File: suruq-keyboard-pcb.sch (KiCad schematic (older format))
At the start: 19 parts

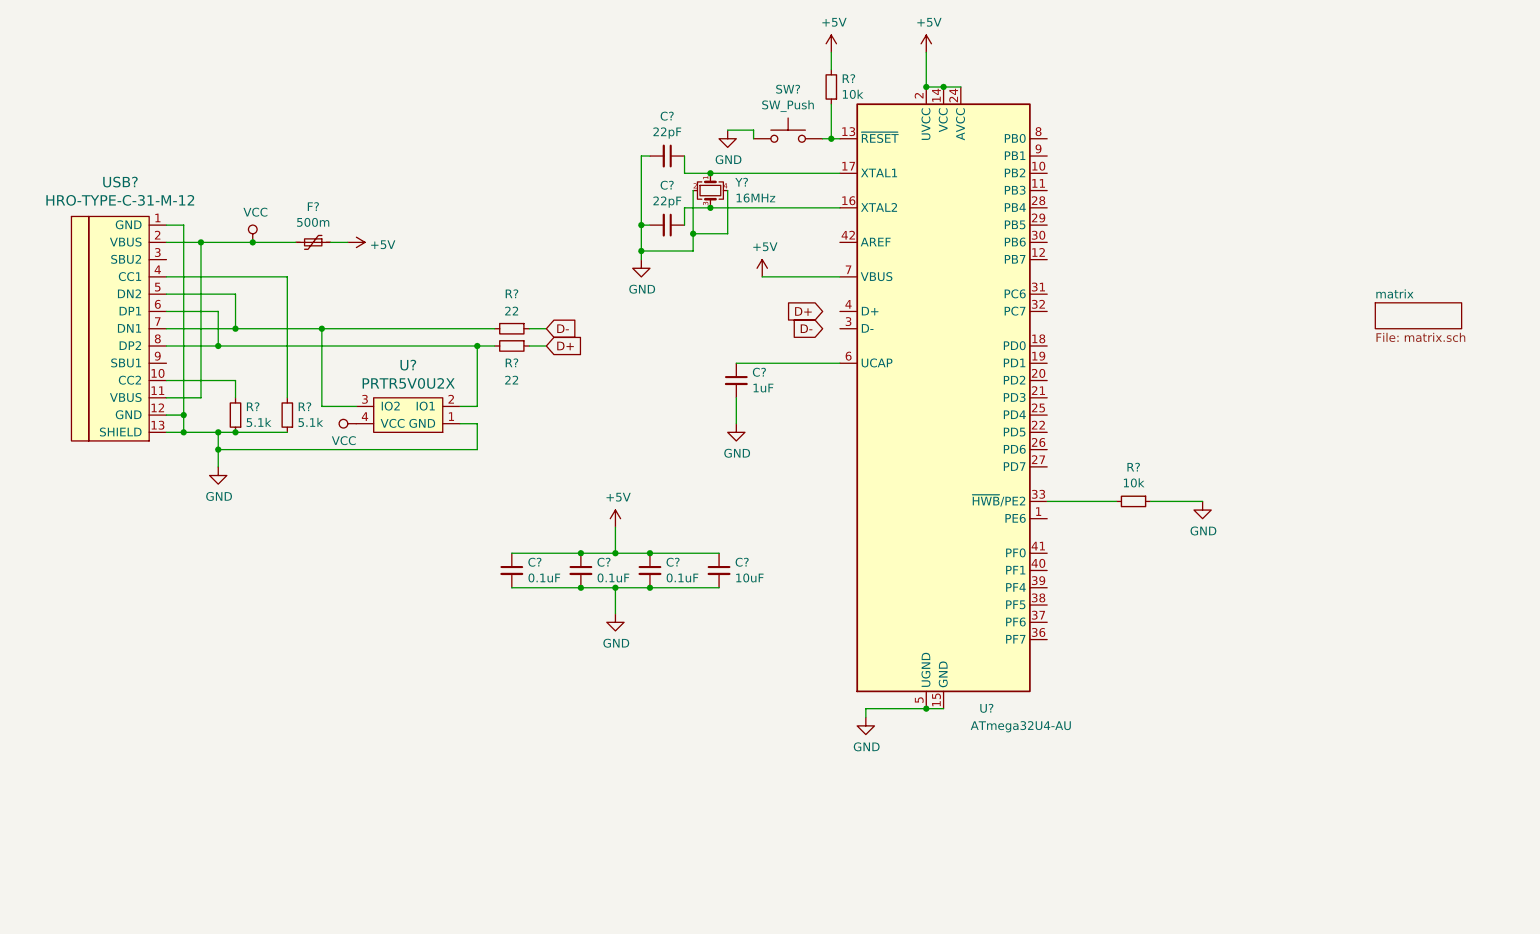
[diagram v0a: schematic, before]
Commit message: change layout and matrix
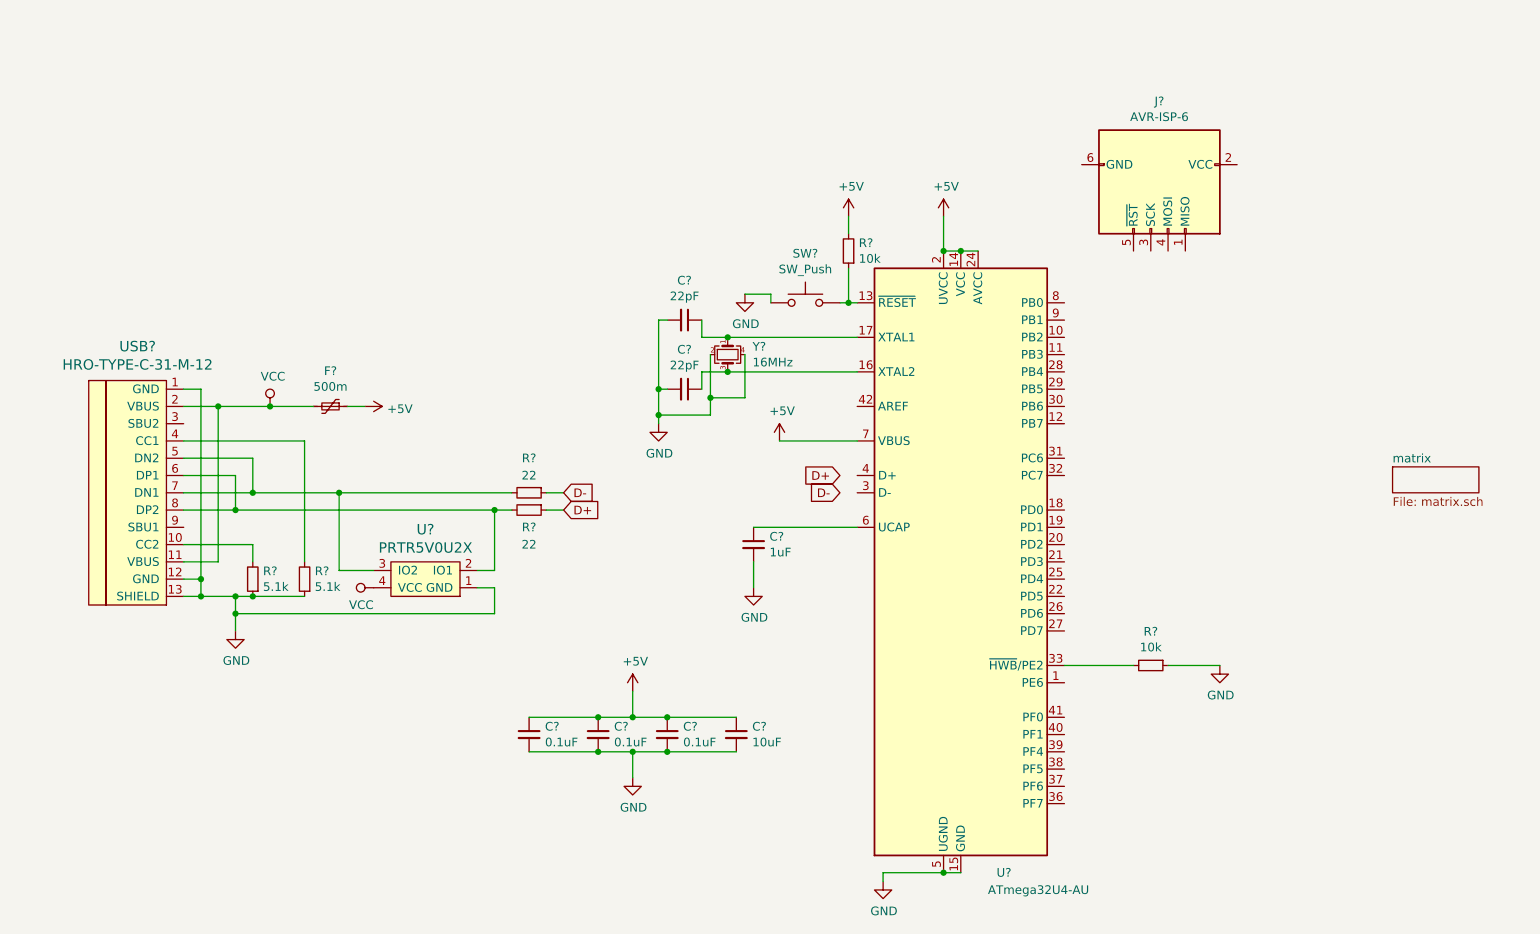
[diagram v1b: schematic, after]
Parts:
- added J?: AVR-ISP-6, symbol Connector:AVR-ISP-6
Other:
- moved on the sheet: C?, F?, R?, SW?, U?, USB?, Y?

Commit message: pcb layout routing WIP
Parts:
- C1, C2, C3, C4, C5, C6, C7: renamed from C?; footprint (none) -> Capacitor_SMD:C_0805_2012Metric_Pad1.15x1.40mm_HandSolder
- F1: renamed from F?; footprint (none) -> Fuse:Fuse_1206_3216Metric_Pad1.42x1.75mm_HandSolder
- J1: renamed from J?; footprint (none) -> random-keyboard-parts:Reset_Pretty-Mask
- R1, R2, R3, R4, R5, R6: renamed from R?; footprint (none) -> Resistor_SMD:R_0805_2012Metric_Pad1.15x1.40mm_HandSolder
- SW65: renamed from SW?; footprint (none) -> Button_Switch_Keyboard:SW_Cherry_MX_1.00u_PCB
- U1: renamed from U?; footprint (none) -> random-keyboard-parts:SOT143B
- USB1: renamed from USB?; footprint (none) -> Type-C:HRO-TYPE-C-31-M-12-HandSoldering
- Y1: renamed from Y?; footprint (none) -> Crystal:Crystal_SMD_3225-4Pin_3.2x2.5mm_HandSoldering
- gave numbers to parts that had none: 1
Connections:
- net +5V: now also J1.2 (VCC)
- net D+: now also U2.4 (D+)
- net D-: now also U2.3 (D-)
- net GND: now also J1.6 (GND)
- net row0: now reaches U2.1 (PE6)
- net rot_out: now reaches U2.11 (PB3)
- net Reset: now reaches R5.1, SW65.2, U2.13 (~RESET)
- net Reset: now also J1.5 (~RST)
- net fad_out: now reaches U2.18 (PD0)
- net col8: now reaches U2.19 (PD1)
- net col9: now reaches U2.20 (PD2)
- net col10: now reaches U2.21 (PD3)
- net col11: now reaches U2.22 (PD5)
- net col12: now reaches U2.25 (PD4)
- net col13: now reaches U2.26 (PD6)
- net col14: now reaches U2.27 (PD7)
- net col0: now reaches U2.28 (PB4)
- net col1: now reaches U2.29 (PB5)
- net col2: now reaches U2.30 (PB6)
- net col3: now reaches U2.31 (PC6)
- net col4: now reaches U2.32 (PC7)
- net col6: now reaches U2.36 (PF7)
- net col5: now reaches U2.37 (PF6)
- net row1: now reaches U2.38 (PF5)
- net row4: now reaches U2.39 (PF4)
- net row3: now reaches U2.40 (PF1)
- net row2: now reaches U2.41 (PF0)
- net col7: now reaches U2.8 (PB0)
- net DN: now reaches R3.2, U1.3 (IO2), USB1.5 (DN2), USB1.7 (DN1)
- net DP: now reaches R4.2, U1.2 (IO1), USB1.6 (DP1), USB1.8 (DP2)
- net MISO: now reaches J1.1 (MISO)
- net SCK: now reaches J1.3 (SCK)
- net MOSI: now reaches J1.4 (MOSI)
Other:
- moved on the sheet: F1, J1, R5, SW65

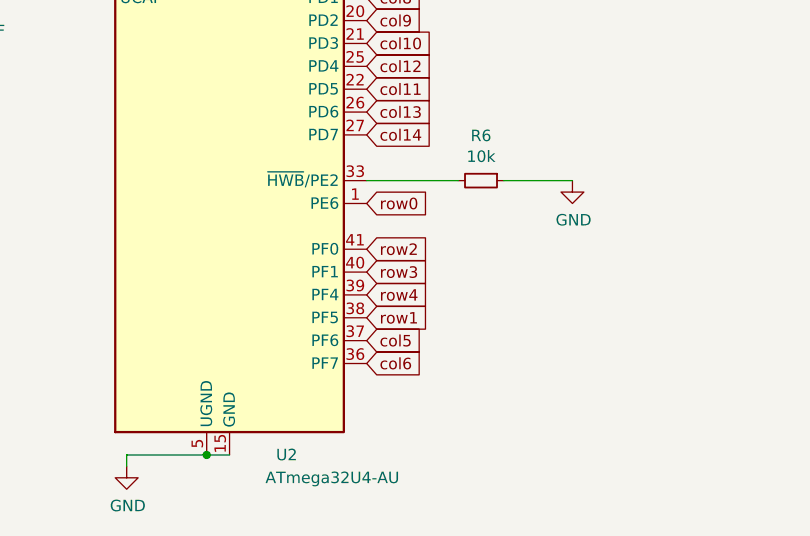
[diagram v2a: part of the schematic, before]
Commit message: routing gauche et MCU
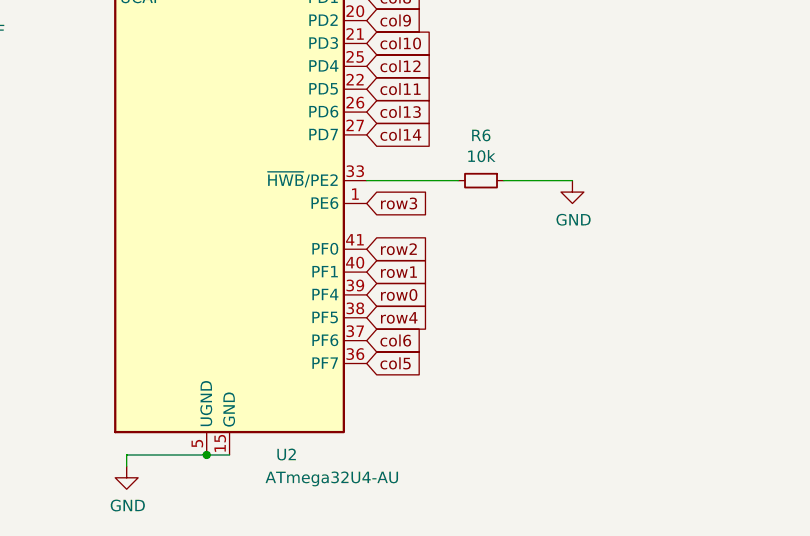
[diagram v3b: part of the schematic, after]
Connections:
- net col5: now also U2.36 (PF7); no longer U2.37 (PF6)
- net col6: now also U2.37 (PF6); no longer U2.36 (PF7)
- net row0: now also U2.39 (PF4); no longer U2.1 (PE6)
- net row1: now also U2.40 (PF1); no longer U2.38 (PF5)
- net row3: now also U2.1 (PE6); no longer U2.40 (PF1)
- net row4: now also U2.38 (PF5); no longer U2.39 (PF4)
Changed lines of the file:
@@
 Text GLabel 6700 4250 2    50   Input ~ 0
 col14
-Text GLabel 6700 4550 2    50   Input ~ 0
+Text GLabel 6700 4950 2    50   Input ~ 0
 row0
 Text GLabel 6700 4750 2    50   Input ~ 0
 row2
+Text GLabel 6700 4550 2    50   Input ~ 0
+row3
+Text GLabel 6700 5050 2    50   Input ~ 0
+row4
 Text GLabel 6700 4850 2    50   Input ~ 0
-row3
-Text GLabel 6700 4950 2    50   Input ~ 0
-row4
-Text GLabel 6700 5050 2    50   Input ~ 0
 row1
+Text GLabel 6700 5250 2    50   Input ~ 0
+col5
 Text GLabel 6700 5150 2    50   Input ~ 0
-col5
-Text GLabel 6700 5250 2    50   Input ~ 0
 col6
 Text GLabel 6700 3550 2    50   Input ~ 0

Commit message: fin routing
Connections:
- net col14 is gone; now on net col13: U2.27 (PD7)
- net MISO: now also U2.9 (PB1)
- net MOSI: now also U2.10 (PB2)
- net SCK: now also U2.11 (PB3)
- net col10: now also U2.22 (PD5); no longer U2.21 (PD3)
- net col11: now also U2.25 (PD4); no longer U2.22 (PD5)
- net col12: now also U2.26 (PD6); no longer U2.25 (PD4)
- net col13: no longer U2.26 (PD6)
- net col8: now also U2.20 (PD2); no longer U2.19 (PD1)
- net col9: now also U2.21 (PD3); no longer U2.20 (PD2)
- net fad_out: now also U2.19 (PD1); no longer U2.18 (PD0)
- net rot_out: now also U2.18 (PD0); no longer U2.11 (PB3)
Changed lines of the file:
@@
 Text GLabel 7400 1750 3    50   Input ~ 0
 MISO
-Text GLabel 7300 1750 3    50   Input ~ 0
-MOSI
 Text GLabel 7200 1750 3    50   Input ~ 0
 SCK
@@
 Text GLabel 6700 3350 2    50   Input ~ 0
 col4
-Text GLabel 6700 3650 2    50   Input ~ 0
+Text GLabel 6700 3750 2    50   Input ~ 0
 col8
-Text GLabel 6700 3750 2    50   Input ~ 0
+Text GLabel 6700 3850 2    50   Input ~ 0
 col9
-Text GLabel 6700 3850 2    50   Input ~ 0
+Text GLabel 6700 4050 2    50   Input ~ 0
 col10
+Text GLabel 6700 4150 2    50   Input ~ 0
+col12
 Text GLabel 6700 3950 2    50   Input ~ 0
-col12
-Text GLabel 6700 4050 2    50   Input ~ 0
 col11
-Text GLabel 6700 4150 2    50   Input ~ 0
+Text GLabel 6700 4250 2    50   Input ~ 0
 col13
-Text GLabel 6700 4250 2    50   Input ~ 0
-col14
 Text GLabel 6700 4950 2    50   Input ~ 0
 row0
@@
 Text GLabel 6700 5150 2    50   Input ~ 0
 col6
+Text GLabel 6700 3650 2    50   Input ~ 0
+fad_out
 Text GLabel 6700 3550 2    50   Input ~ 0
-fad_out
-Text GLabel 6700 2650 2    50   Input ~ 0
 rot_out
 $Comp
@@
 Text GLabel 2100 3450 1    50   Input ~ 0
 DN
+Text GLabel 6700 2650 2    50   Input ~ 0
+SCK
+Text GLabel 7300 1750 3    50   Input ~ 0
+MOSI
+Text GLabel 6700 2550 2    50   Input ~ 0
+MOSI
+Text GLabel 6700 2450 2    50   Input ~ 0
+MISO
 $EndSCHEMATC

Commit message: add silk screen, Fader65
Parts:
- SW65: footprint Button_Switch_Keyboard:SW_Cherry_MX_1.00u_PCB -> Button_Switch_SMD:SW_SPST_SKQG_WithStem
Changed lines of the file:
@@
 F 0 "SW65" H 4700 1835 50  0000 C CNN
 F 1 "SW_Push" H 4700 1744 50  0000 C CNN
-F 2 "Button_Switch_Keyboard:SW_Cherry_MX_1.00u_PCB" H 4700 1750 50  0001 C CNN
+F 2 "Button_Switch_SMD:SW_SPST_SKQG_WithStem" H 4700 1750 50  0001 C CNN
 F 3 "~" H 4700 1750 50  0001 C CNN
 	1    4700 1550
